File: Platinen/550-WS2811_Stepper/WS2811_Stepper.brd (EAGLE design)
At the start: 71.4 x 38.7 mm, 50 parts, among them CON1 End SW1, CON2 End SW2, CON3 End SW1H, CON4 STEPPER_CON, CON5 End SW2H, CON6 NEMA17, CON7 LED, IC1 4017N, J10 MiniStp1, M1 BOARD_A4988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

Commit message: 6-pin Stepper Conector
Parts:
- J10: value MiniStp1 -> (none); device Pfostenstecker_4_u_6:CON-HARTING-ML_ML4 -> con-harting-ml:ML6
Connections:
- removed net N$15: C3.1, CON7.2, JP1.3, JP2.3, JP3.3, R5.1, U2R.3, U3H.3
- new net LED: C3.1, CON7.2, J10.6, JP1.3, JP2.3, JP3.3, R5.1, U2R.3, U3H.3
- net +5V: now also J10.5
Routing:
- net LED: track 0.00 -> 89.0 mm
- net N$15: track 79.8 -> 0.00 mm
- net +5V: track 149.2 -> 154.0 mm
- net N$40: track 53.2 -> 55.3 mm

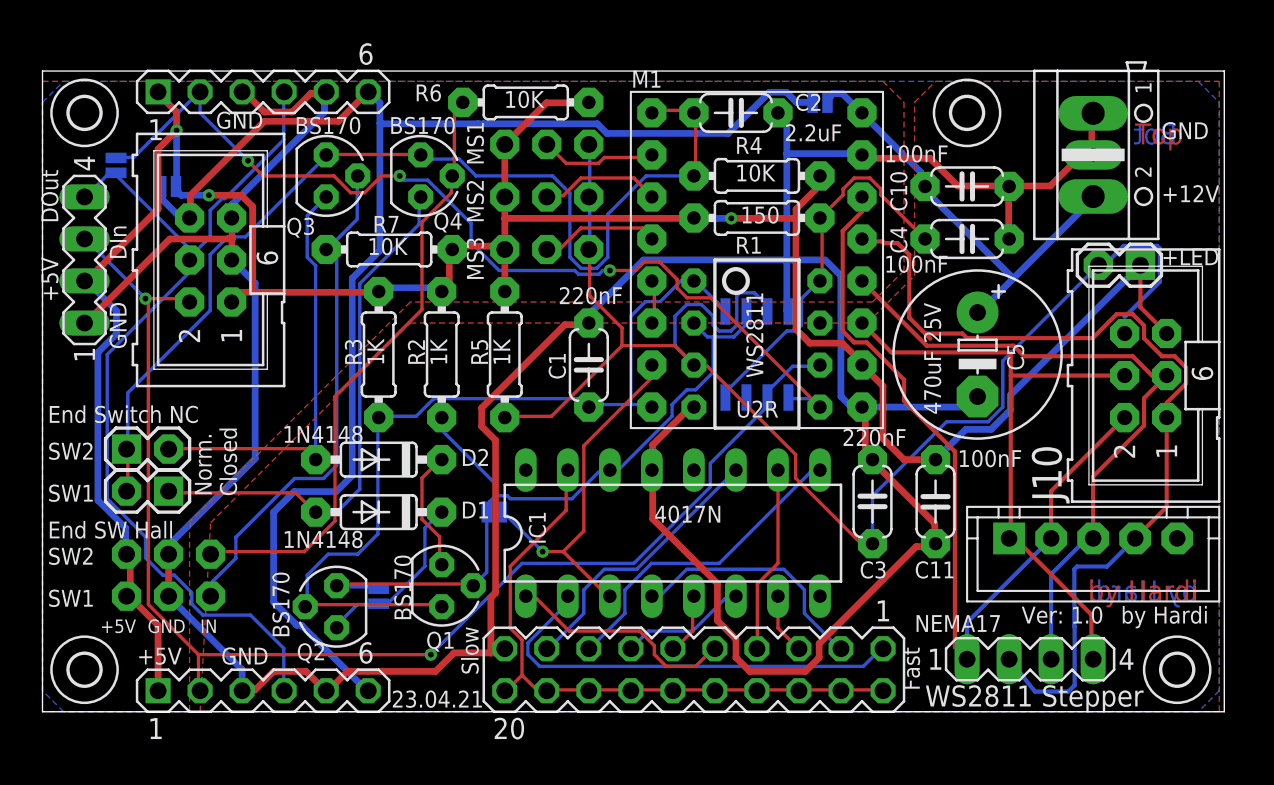
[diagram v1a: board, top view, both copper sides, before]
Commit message: Corrected 6=12V Jumper
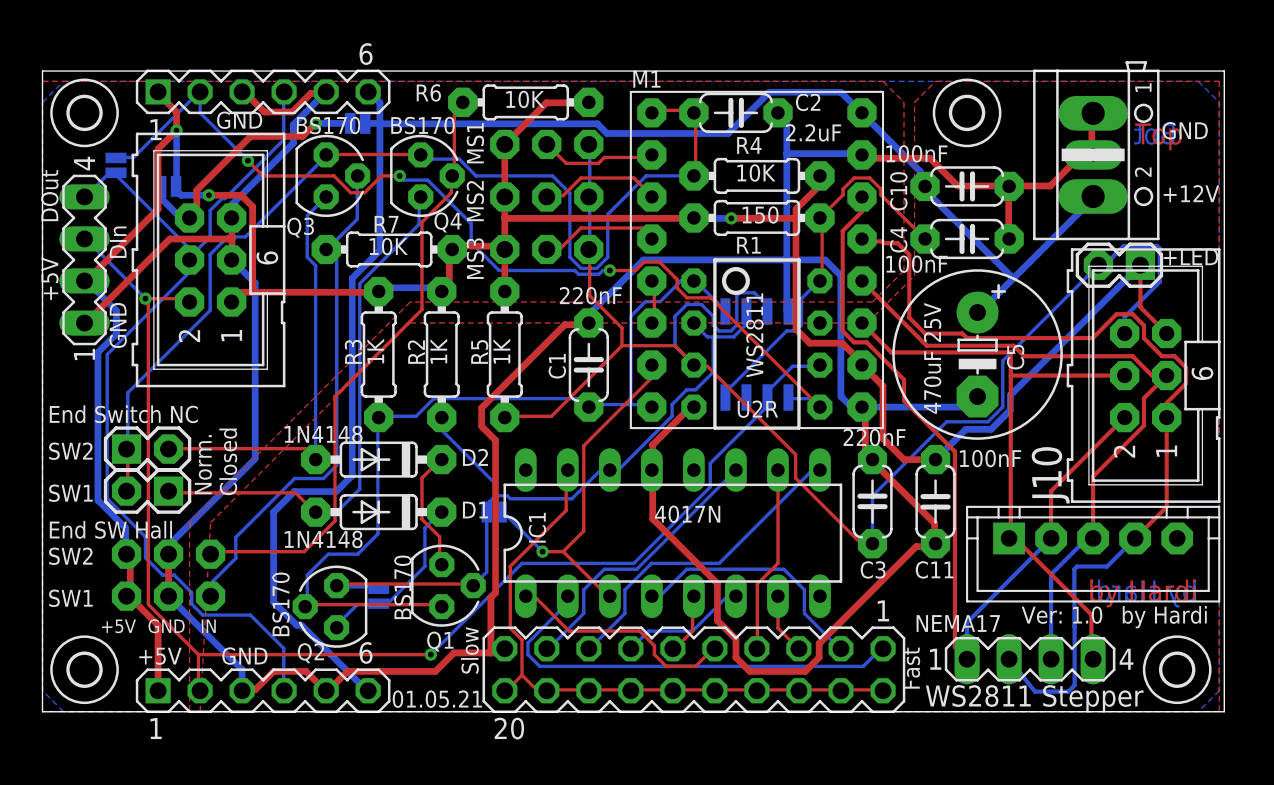
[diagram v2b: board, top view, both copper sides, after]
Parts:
- moved 6=12V 28.0 mm to (19.1, 35.6), turned to 0 degrees
- renumbered O1 to IN
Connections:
- removed net N$12: 6=12V.2, C10.1, C5.+, M1.VMOT, X1.2
- new net N$15: 6=12V.2, 6=5V.1, IN.6
- net N$7: now also C10.1, C5.+, M1.VMOT, X1.2; no longer 6=5V.1, IN.6
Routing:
- net N$12: track 26.7 -> 0.00 mm
- net N$15: track 0.00 -> 15.7 mm, vias 0 -> 1
- net N$7: track 88.5 -> 98.9 mm
- net LED: track 89.0 -> 90.0 mm
